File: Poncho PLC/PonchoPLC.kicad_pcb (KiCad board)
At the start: 2 copper layers, 85.7 x 137.2 mm, 137 parts, among them J1 I2C, J10 TB_1X3, J11 TB_1X3, J2 RS-232, J3 TB_1X3, J4 TB_1X3, J5 TB_1X2, J6 TB_1X2, J7 TB_1X2, J8 TB_1X3, J9 TB_1X3, K1 RELAY_C, K2 RELAY_C, K3 RELAY_C, K4 RELAY_C, P1 CONN_02X20, P10 CONN_01X20, P11 CONN_01X20, P12 CONN_01X06, P13 CONN_01X06, P14 CONN_02X12, P15 CONN_02X12, P16 CONN_02X12, P17 CONN_02X12, P18 CONN_01X12, P19 CONN_01X12, P2 CONN_01X20, P20 CONN_01X12, P21 CONN_01X12, P3 CONN_02X20, P4 CONN_02X20, P5 CONN_01X19, P6 CONN_02X20, P7 CONN_01X20, P8 CONN_02X20, P9 CONN_02X20, Q1 FQT13N06L, Q2 FQT13N06L, Q3 FQT13N06L, Q4 FQT13N06L, Q5 2N7002, Q6 2N7002, Q7 2N7002, Q8 2N7002, U1 TLP627-4, U2 TLP627-4, U3 MCP1416, U4 MCP1416, U5 MCP1416, U6 MCP1416

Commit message: Borro pistas y footprints del modelo, edito textos y separo componentes automáticamente por hojas.
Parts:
- removed G***: LOGO, Poncho_Esqueleto:Logo_Poncho
- removed G***: Logo_EDU-CIAA, Poncho_Esqueleto:Logo_EDU-CIAA
- removed G101: Logo_OSHWA, Poncho_Esqueleto:Logo_OSHWA
- removed P1, P3, P4, P6, P8, P9: CONN_02X20, Pin_Headers:Pin_Header_Straight_2x20
- removed P10, P11: CONN_01X20, Pin_Headers:Pin_Header_Straight_1x20
- removed P12, P13: CONN_01X06, mod:bornier6
- removed P14, P15, P16, P17: CONN_02X12, Pin_Headers:Pin_Header_Straight_2x12
- removed P18, P19, P20, P21: CONN_01X12, Pin_Headers:Pin_Header_Straight_1x12
- removed P2, P7: CONN_01X20, Pin_Headers:Pin_Header_Straight_2x12
- removed P5: CONN_01X19, Pin_Headers:Pin_Header_Straight_1x19
- moved R11 273.2 mm to (363.0, 54.8)
- moved R25 271.4 mm to (358.8, 50.3)
- moved R20 271.3 mm to (363.0, 59.3)
- moved R18 267.7 mm to (357.6, 56.2)
- moved D1 266.0 mm to (353.1, 50.9)
- moved R15 265.8 mm to (357.6, 60.7)
- moved R4 264.0 mm to (357.6, 65.2)
- moved R12 262.9 mm to (352.2, 56.2)
- moved R26 260.9 mm to (352.2, 60.7)
- moved D3 260.7 mm to (347.1, 50.9)
- moved R14 259.0 mm to (352.2, 65.2)
- moved R19 258.0 mm to (346.8, 56.2)
- moved R9 257.2 mm to (352.2, 69.7)
- moved R23 256.0 mm to (346.8, 60.7)
- moved R5 254.1 mm to (346.8, 65.2)
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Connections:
- net /Entradas Optoacopladas/COM renamed GNDD
- net /Salidas Digitales/MOS4 renamed Net-(JP2-Pad2)
- net /Salidas Digitales/MOS5 renamed Net-(JP1-Pad2)
- net /Salidas Digitales/MOS6 renamed Net-(JP3-Pad2)
- net /Salidas Digitales/MOS7 renamed Net-(JP4-Pad2)
- DS1 pad 10: Net-(DS1-Pad10) -> (no net)
- DS1 pad 7: Net-(DS1-Pad7) -> (no net)
- DS1 pad 8: Net-(DS1-Pad8) -> (no net)
- DS1 pad 9: Net-(DS1-Pad9) -> (no net)
- U2 pad 10: Net-(U2-Pad10) -> (no net)
- U2 pad 7: Net-(U2-Pad7) -> (no net)
- U2 pad 8: Net-(U2-Pad8) -> (no net)
- U2 pad 9: Net-(U2-Pad9) -> (no net)
- U3 pad 1: Net-(U3-Pad1) -> (no net)
- U4 pad 1: Net-(U4-Pad1) -> (no net)
- U5 pad 1: Net-(U5-Pad1) -> (no net)
- U6 pad 1: Net-(U6-Pad1) -> (no net)
- XA1 pad 11: /Conector del Poncho/ADC2 -> (no net)
- XA1 pad 13: /Conector del Poncho/ADC1 -> (no net)
- XA1 pad 15: /Conector del Poncho/DAC -> (no net)
- XA1 pad 17: +3.3VADC -> (no net)
- XA1 pad 27: /Conector del Poncho/RD -> (no net)
- XA1 pad 29: /Conector del Poncho/TD -> (no net)
- XA1 pad 3: /Conector del Poncho/RESET -> (no net)
- XA1 pad 41: +3.3VP -> (no net)
- XA1 pad 42: +5VP -> (no net)
- XA1 pad 44: /Conector del Poncho/RXD1 -> (no net)
- XA1 pad 46: /Conector del Poncho/TXEN -> (no net)
- XA1 pad 48: /Conector del Poncho/MDC -> (no net)
- XA1 pad 49: /Conector del Poncho/RXD0 -> (no net)
- XA1 pad 5: /Conector del Poncho/ISP -> (no net)
- XA1 pad 50: /Conector del Poncho/CRS -> (no net)
- XA1 pad 52: /Conector del Poncho/MDIO -> (no net)
- XA1 pad 54: /Conector del Poncho/TXD0 -> (no net)
- XA1 pad 55: /Conector del Poncho/RCLK -> (no net)
- XA1 pad 56: /Conector del Poncho/TXD1 -> (no net)
- XA1 pad 58: /Conector del Poncho/MISO -> (no net)
- XA1 pad 6: /Conector del Poncho/WAKEUP -> (no net)
- XA1 pad 60: /Conector del Poncho/spiSCK -> (no net)
- XA1 pad 61: /Conector del Poncho/MOSI -> (no net)
- XA1 pad 80: /Conector del Poncho/GPIO8 -> (no net)
- XA1 pad 9: /Conector del Poncho/ADC3 -> (no net)
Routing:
- net GND: track 336.4 -> 0.00 mm
- net +5VP: track 64.0 -> 0.00 mm
- net +5V: track 55.4 -> 0.00 mm
- net +3.3VP: track 54.0 -> 0.00 mm
- net +3.3V: track 52.0 -> 0.00 mm
- net GNDA: track 29.5 -> 0.00 mm
- net +3.3VADC: track 14.3 -> 0.00 mm
- net /Circuito Principal/F3: track 11.5 -> 0.00 mm
- net /Circuito Principal/TXD: track 11.5 -> 0.00 mm
- net /Circuito Principal/TD: track 11.5 -> 0.00 mm
- net /Circuito Principal/SDA: track 11.5 -> 0.00 mm
- net /Circuito Principal/SCL: track 11.5 -> 0.00 mm
- net /Circuito Principal/RXD: track 11.5 -> 0.00 mm
- net /Circuito Principal/RESET: track 11.5 -> 0.00 mm
- net /Circuito Principal/RD: track 11.5 -> 0.00 mm
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- removed copper zone on B.Cu, net GND
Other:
- board text added: "PONCHO PLC http://www.proyecto-ciaa.com.ar/"
- board text added: "STACK-UP PCB de xx capas COMPLETAR Stackup"
- board text removed: "PONCHO GRANDE http://www.proyecto-ciaa.com.ar/"

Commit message: Netlist y librería de footprint del proyecto
Generación y carga del archivo de conexiones del proyecto.
Se creo la librería de footprint propia del proyecto y se eliminó las
librerias que se utilizaron de soporte en la etapa inicial.
Se reemplazaron las líneas "model " por "model
${KIPRJMOD}/footprints/EESTN5.3dshapes/" pertenecientes al archivo
.kicad_pcb del proyecto para que se puedan visualizar correctamente los
modelos 3D.
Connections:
- DS1 pad 10: (no net) -> Net-(DS1-Pad10)
- DS1 pad 7: (no net) -> Net-(DS1-Pad7)
- DS1 pad 8: (no net) -> Net-(DS1-Pad8)
- DS1 pad 9: (no net) -> Net-(DS1-Pad9)
- U2 pad 10: (no net) -> Net-(U2-Pad10)
- U2 pad 7: (no net) -> Net-(U2-Pad7)
- U2 pad 8: (no net) -> Net-(U2-Pad8)
- U2 pad 9: (no net) -> Net-(U2-Pad9)
- U3 pad 1: (no net) -> Net-(U3-Pad1)
- U4 pad 1: (no net) -> Net-(U4-Pad1)
- U5 pad 1: (no net) -> Net-(U5-Pad1)
- U6 pad 1: (no net) -> Net-(U6-Pad1)
- XA1 pad 11: (no net) -> /Conector del Poncho/ADC2
- XA1 pad 13: (no net) -> /Conector del Poncho/ADC1
- XA1 pad 15: (no net) -> /Conector del Poncho/DAC
- XA1 pad 17: (no net) -> +3.3VADC
- XA1 pad 27: (no net) -> /Conector del Poncho/RD
- XA1 pad 29: (no net) -> /Conector del Poncho/TD
- XA1 pad 3: (no net) -> /Conector del Poncho/RESET
- XA1 pad 41: (no net) -> +3.3VP
- XA1 pad 42: (no net) -> +5VP
- XA1 pad 44: (no net) -> /Conector del Poncho/RXD1
- XA1 pad 46: (no net) -> /Conector del Poncho/TXEN
- XA1 pad 48: (no net) -> /Conector del Poncho/MDC
- XA1 pad 49: (no net) -> /Conector del Poncho/RXD0
- XA1 pad 5: (no net) -> /Conector del Poncho/ISP
- XA1 pad 50: (no net) -> /Conector del Poncho/CRS
- XA1 pad 52: (no net) -> /Conector del Poncho/MDIO
- XA1 pad 54: (no net) -> /Conector del Poncho/TXD0
- XA1 pad 55: (no net) -> /Conector del Poncho/RCLK
- XA1 pad 56: (no net) -> /Conector del Poncho/TXD1
- XA1 pad 58: (no net) -> /Conector del Poncho/MISO
- XA1 pad 6: (no net) -> /Conector del Poncho/WAKEUP
- XA1 pad 60: (no net) -> /Conector del Poncho/spiSCK
- XA1 pad 61: (no net) -> /Conector del Poncho/MOSI
- XA1 pad 80: (no net) -> /Conector del Poncho/GPIO8
- XA1 pad 9: (no net) -> /Conector del Poncho/ADC3
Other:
- board text removed: "STACK-UP PCB de xx capas COMPLETAR Stackup"

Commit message: Avance posicionamiento
Posicionamiento de las salidas digitales a relé.
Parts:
- moved Q6 249.2 mm to (44.3, 51.0), turned to 90 degrees
- moved R39 247.1 mm to (48.2, 51.0), turned to 270 degrees
- moved D18 242.2 mm to (43.9, 109.7), turned to 270 degrees
- moved Q8 239.3 mm to (44.3, 67.6), turned to 90 degrees
- moved R41 235.9 mm to (45.3, 55.5), turned to 180 degrees
- moved D17 229.7 mm to (46.8, 76.7), turned to 90 degrees
- moved J10 228.9 mm to (16.4, 103.2), turned to 270 degrees
- moved R45 228.0 mm to (45.3, 72.1), turned to 180 degrees
- moved R40 227.8 mm to (45.3, 88.5), turned to 180 degrees
- moved D15 225.0 mm to (43.9, 60.1), turned to 270 degrees
- moved Q7 222.4 mm to (44.3, 100.4), turned to 90 degrees
- moved J9 221.4 mm to (16.4, 72.7), turned to 270 degrees
- moved J8 219.0 mm to (16.4, 57.4), turned to 270 degrees
- moved R43 218.9 mm to (48.2, 67.6), turned to 270 degrees
- moved D13 218.0 mm to (46.8, 60.1), turned to 90 degrees
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- renumbered D19 to D111, K3 to K11

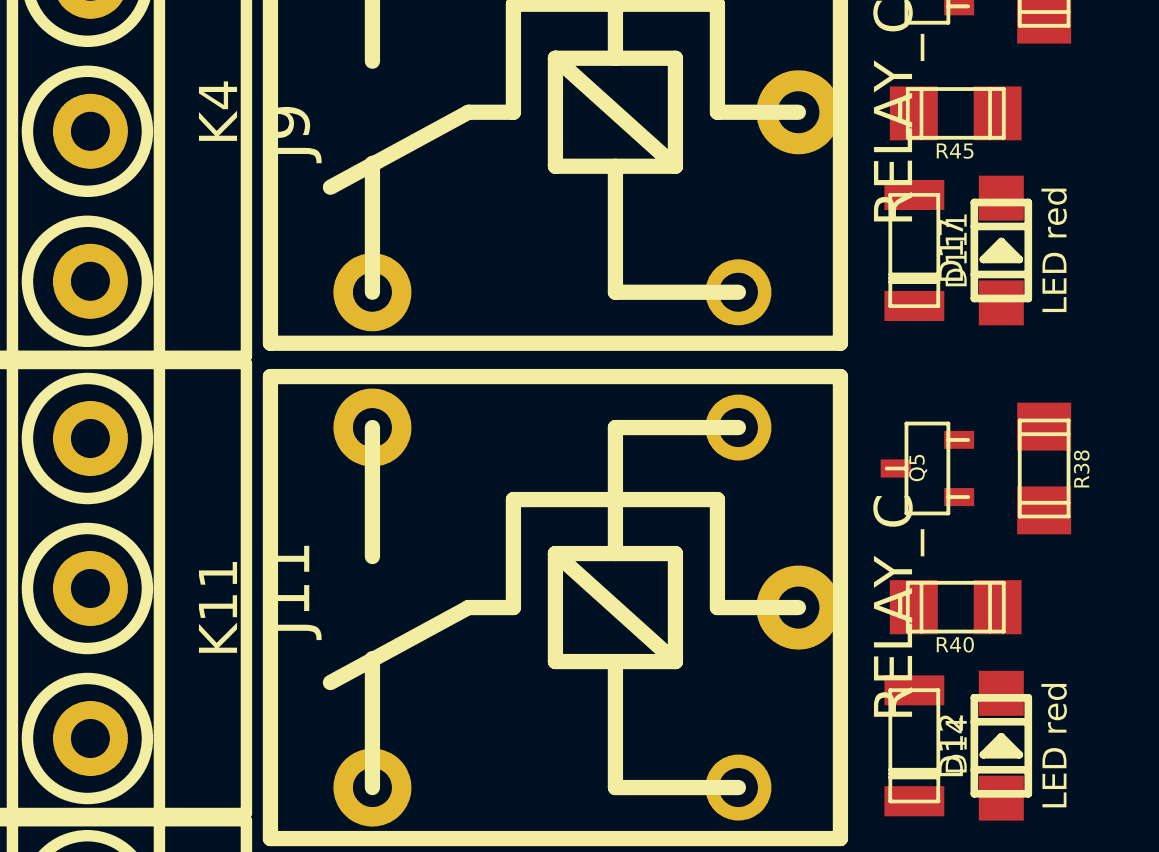
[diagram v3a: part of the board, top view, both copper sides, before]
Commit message: Cambio SCH
Se modificaron algunas etiquetas para beneficiar el routeo del pcb en la
conexión Rele-Bornera.
Se actualizaron las referencias de las huellas de la librería anterior a
la actual, para lograr compatibilidad en el netlist y poder cargarlo al
pcb.
Se actualizaron los filtros de búsqueda de huellas en algunos
componentes de la librería de sch.
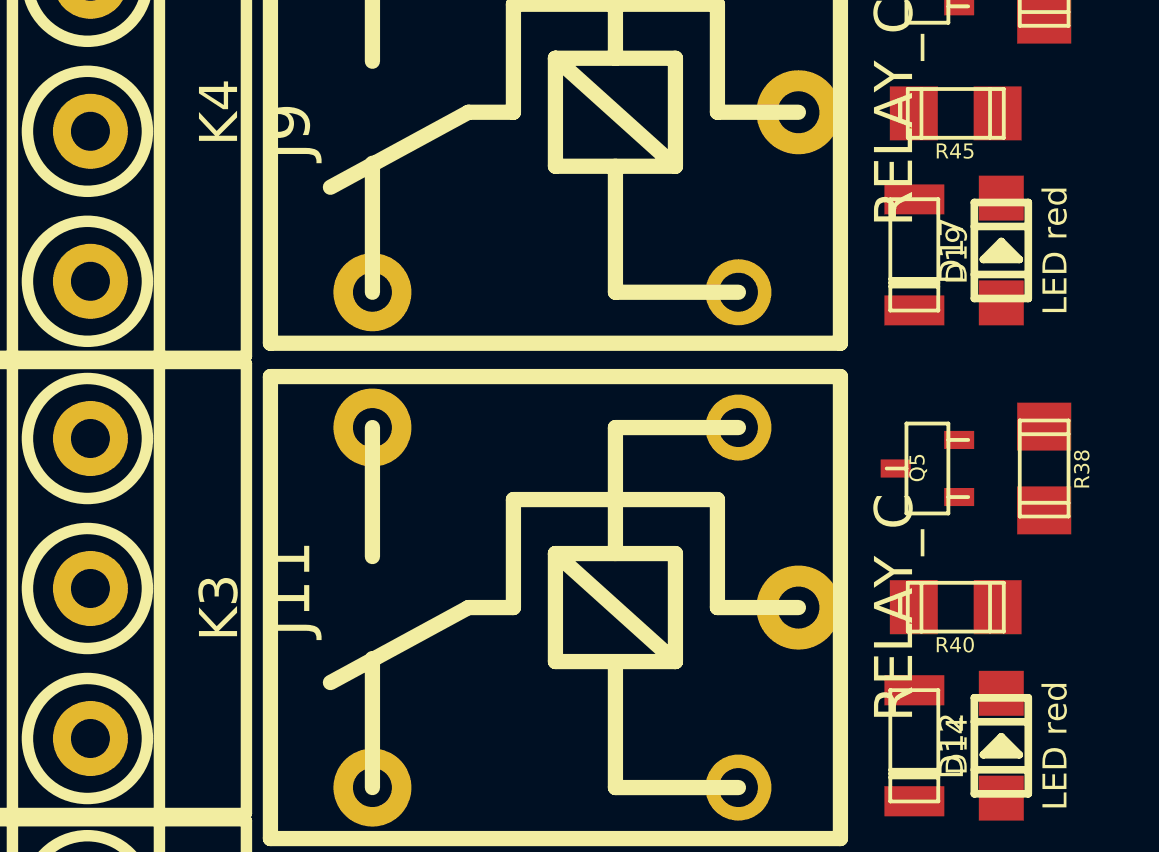
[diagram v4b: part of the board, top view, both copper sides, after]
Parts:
- removed D111: LL4148, EESTN5:SOD80C
- removed K11: RELAY_C, EESTN5:Relay_C
- added D19: LL4148, Poncho-PLC:SOD80C, F.Cu at (43.9, 76.8)
- added K3: RELAY_C, Poncho-PLC:Relay_C, F.Cu at (31.9, 88.6)
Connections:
- J10 pad 1: /Salidas Digitales/NC1C -> /Salidas Digitales/NO1C
- J10 pad 2: /Salidas Digitales/NO1C -> /Salidas Digitales/C1C
- J10 pad 3: /Salidas Digitales/C1C -> /Salidas Digitales/NC1C
- J11 pad 1: /Salidas Digitales/NC1D -> /Salidas Digitales/NO1D
- J11 pad 2: /Salidas Digitales/NO1D -> /Salidas Digitales/C1D
- J11 pad 3: /Salidas Digitales/C1D -> /Salidas Digitales/NC1D
- J8 pad 1: /Salidas Digitales/NC1A -> /Salidas Digitales/NO1A
- J8 pad 2: /Salidas Digitales/NO1A -> /Salidas Digitales/C1A
- J8 pad 3: /Salidas Digitales/C1A -> /Salidas Digitales/NC1A
- J9 pad 1: /Salidas Digitales/NC1B -> /Salidas Digitales/NO1B
- J9 pad 2: /Salidas Digitales/NO1B -> /Salidas Digitales/C1B
- J9 pad 3: /Salidas Digitales/C1B -> /Salidas Digitales/NC1B

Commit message: Avance posicionamiento
Posicione las borneras de las entradas digitales.
Arregle el footprint de las borneras para que tengan un pitch de 100mils
Cambie a bottom layer algunos componentes para acercarme a un tamaño de
placa de 150X100mm
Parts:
- D17, D18, Q7, Q8, R10, R11, R12, R13, R14, R15, R2, R3, R4, R44, R45, R5, R6, R7, R8, R9: moved to B.Cu
- J3, J4: footprint EESTN5:BORNERA3 -> Poncho-PLC:BORNERA3
- J5: footprint EESTN5:BORNERA2 -> Poncho-PLC:BORNERA2
- J6, J7: footprint EESTN5:BORNERA3 -> Poncho-PLC:BORNERA2
- moved J6 214.3 mm to (47.2, 147.6), turned to 270 degrees
- moved J7 196.8 mm to (47.1, 137.4), turned to 270 degrees
- moved R11 195.0 mm to (180.9, 124.4)
- moved R4 187.2 mm to (180.9, 126.9)
- moved R9 183.2 mm to (180.9, 134.4)
- moved R12 182.6 mm to (180.9, 119.3)
- moved R15 182.0 mm to (180.9, 104.1)
- moved R14 177.0 mm to (180.8, 109.2)
- moved R5 175.3 mm to (180.9, 121.8)
- moved R10 174.9 mm to (180.9, 129.4)
- moved R2 170.2 mm to (180.9, 136.9)
- moved R7 166.8 mm to (180.9, 111.9)
- moved R3 163.0 mm to (180.9, 131.9)
- moved J5 157.9 mm to (187.7, 103.8), turned to 90 degrees
- moved R8 156.3 mm to (180.9, 106.6)
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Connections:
- D1 pad 2: /Conector del Poncho/COL0 -> /Conector del Poncho/COL1
- D2 pad 2: /Conector del Poncho/COL1 -> /Conector del Poncho/COL2
- D3 pad 2: /Conector del Poncho/COL2 -> /Entradas Optoacopladas/DIN2
- D5 pad 2: /Entradas Optoacopladas/DIN4 -> /Conector del Poncho/COL0
- R17 pad 1: /Conector del Poncho/COL0 -> /Conector del Poncho/COL1
- R19 pad 1: /Conector del Poncho/COL1 -> /Conector del Poncho/COL2
- R21 pad 1: /Conector del Poncho/COL2 -> /Entradas Optoacopladas/DIN2
- R25 pad 1: /Entradas Optoacopladas/DIN4 -> /Conector del Poncho/COL0
- U1 pad 12: /Conector del Poncho/COL2 -> /Entradas Optoacopladas/DIN2
- U1 pad 14: /Conector del Poncho/COL1 -> /Conector del Poncho/COL2
- U1 pad 16: /Conector del Poncho/COL0 -> /Conector del Poncho/COL1
- U2 pad 16: /Entradas Optoacopladas/DIN4 -> /Conector del Poncho/COL0
- XA1 pad 33: /Entradas Optoacopladas/DIN3 -> /Entradas Optoacopladas/DIN2
- XA1 pad 36: /Entradas Optoacopladas/DIN4 -> /Entradas Optoacopladas/DIN3
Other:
- board size 85.7 x 137.2 mm -> 150 x 137.2 mm

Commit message: Avance posicionamiento & Dimensión del poncho
Se avanzo en el posicionamiento de las entradas.
Se esta evaluando la dimensión del poncho y la posición de los agujeros
de sujeción.
A partir de ahora el diseño esta a cargo del Alumno Ignacio Vetrano
(E.E.S.T. N°5 - 5to 5ta)
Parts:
- D14, D15, Q5, Q6, R40, R41, U3: moved to B.Cu
- J10, J11, J8, J9: footprint EESTN5:BORNERA3 -> Poncho-PLC:BORNERA3
- moved D9 220.3 mm to (57.6, 145.0)
- moved R30 218.6 mm to (64.0, 146.1)
- moved Q1 213.1 mm to (61.1, 141.7)
- moved R34 209.2 mm to (57.1, 149.7), turned to 90 degrees
- moved TH1 189.2 mm to (65.6, 150.2)
- moved JP2 131.2 mm to (60.2, 154.7)
- moved U3 129.6 mm to (60.2, 149.4)
- moved R38 17.6 mm to (75.1, 106.9)
- moved D16 16.6 mm to (75.1, 99.0)
- moved D18 16.6 mm to (75.2, 99.1)
- moved Q7 16.6 mm to (75.3, 89.2)
- moved R42 16.6 mm to (75.2, 90.6)
- moved R44 16.6 mm to (75.2, 93.8)
- moved D14 16.5 mm to (75.1, 115.7)
- moved D12 16.5 mm to (75.1, 115.4)
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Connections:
- TH1 pad 2: Net-(J6-Pad1) -> Net-(J6-Pad2)
- TH2 pad 2: Net-(J6-Pad2) -> Net-(J6-Pad1)
- TH3 pad 2: Net-(J7-Pad1) -> Net-(J7-Pad2)
- TH4 pad 2: Net-(J7-Pad2) -> Net-(J7-Pad1)
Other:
- net class Default: via_dia 0.6 -> 1.5; via_drill 0.4 -> 0.5
- rule via_min_drill: 0.3 -> 0.5
- rule via_min_size: 0.4 -> 1.5

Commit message: tamaño placa
Se ajusto el tamaño de la placa a 100x150mm.
Avance en posicionamiento.
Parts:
- U4: moved to B.Cu
- moved U4 226.9 mm to (65.3, 106.9), turned to 270 degrees
- moved C6 220.7 mm to (65.3, 112.7), turned to 180 degrees
- moved R35 216.6 mm to (61.3, 118.9), turned to 270 degrees
- moved C1 214.1 mm to (58.4, 119.1), turned to 270 degrees
- moved R31 213.0 mm to (69.4, 117.7), turned to 90 degrees
- moved D10 198.9 mm to (65.2, 120.3)
- moved Q2 198.6 mm to (58.3, 113.2), turned to 90 degrees
- moved R32 197.5 mm to (77.5, 133.5), turned to 90 degrees
- moved C5 186.6 mm to (72.0, 128.5), turned to 90 degrees
- moved JP1 184.3 mm to (65.2, 115.5), turned to 180 degrees
- moved TH2 176.6 mm to (55.2, 118.9), turned to 90 degrees
- moved C2 158.0 mm to (65.3, 109.9)
- moved Q4 97.4 mm to (300.8, 95.4)
- moved C3 97.4 mm to (298.5, 114.9)
- moved C8 97.4 mm to (302.2, 105.3)
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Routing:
- net +5V: track 0.00 -> 57.4 mm
- net GND: track 0.00 -> 36.3 mm, vias 0 -> 1
- net /Salidas Digitales/C1C: track 0.00 -> 24.5 mm
- net /Salidas Digitales/C1D: track 0.00 -> 24.2 mm
- net /Salidas Digitales/C1B: track 0.00 -> 24.0 mm
- net /Salidas Digitales/C1A: track 0.00 -> 23.6 mm
- net Net-(JP1-Pad2): track 0.00 -> 15.7 mm
- net Net-(J6-Pad1): track 0.00 -> 13.9 mm
- net /Salidas Digitales/DOUT5: track 0.00 -> 13.7 mm
- net Net-(Q2-Pad2): track 0.00 -> 11.1 mm
- net /Salidas Digitales/NC1C: track 0.00 -> 10.7 mm
- net Net-(Q1-Pad2): track 0.00 -> 10.5 mm
- net /Salidas Digitales/NC1D: track 0.00 -> 10.4 mm
- net /Salidas Digitales/NC1B: track 0.00 -> 10.2 mm
- net /Salidas Digitales/NO1C: track 0.00 -> 9.95 mm
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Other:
- board size 150 x 137.2 mm -> 150 x 99.7 mm
- net class Default: clearance 0.508 -> 0.254; via_dia 1.5 -> 1.016
- rule trace_clearance: 0.508 -> 0.254
- rule trace_min: 0.2 -> 0.2032
- rule via_min_size: 1.5 -> 1.016

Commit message: Avance posicionamiento
Se avanzo en el posicionamiento de componentes.
Se actualizo el modelo 3D de varios componentes.
Se agregaron los logos de la escuela y de Open Hardware.
Falta actualizar las librerias del repositorio y las rutas relativas de
los modelos 3D para que la vista 3D sea portable a cualquier pc.
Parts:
- added G1: LOGO, EESTN5:LOGO_EESTN5, F.Cu at (179.0, 66.6)
- added G2: LOGO, Logo_silk_OSHW_12x13mm, F.Cu at (178.4, 52.8)
- C1, C2, C3, C4, C5, C6, C7, C8: footprint EESTN5:C_1206 -> Poncho-PLC:C_1206
- D1, D10, D11, D12, D13, D16, D2, D3, D4, D5, D6, D7, D8, D9: footprint EESTN5:LED_1206 -> Poncho-PLC:LED_1206
- D14, D15, D18: footprint EESTN5:SOD80C -> Poncho-PLC:SOD80C
- D17: footprint EESTN5:LED_1206 -> Poncho-PLC:LED_1206; moved to F.Cu
- D19: moved to B.Cu
- DS1: footprint EESTN5:LCD_16x2 -> Poncho-PLC:LCD_16x2
- J1: footprint EESTN5:HEADER-4H -> EESTN5:JST-4V
- J2: footprint EESTN5:HEADER-4H -> Poncho-PLC:HEADER-4H; moved to B.Cu
- JP1, JP2, JP3, JP4: footprint EESTN5:Pin_strip_2 -> Poncho-PLC:Pin_strip_2
- K1, K2, K4: footprint EESTN5:Relay_C -> Poncho-PLC:Relay_C
- Q1, Q2, Q3, Q4: footprint EESTN5:SOT-223 -> Poncho-PLC:SOT-223; moved to B.Cu
- Q5, Q6, Q7, Q8: footprint EESTN5:SOT23 -> Poncho-PLC:SOT23
- R1, R17, R19, R21, R23, R25, R27, R29, R30, R31, R32, R33: footprint EESTN5:R_1206 -> Poncho-PLC:R_1206; moved to B.Cu
- R10, R11, R12, R13, R14, R15, R16, R18, R2, R20, R22, R24, R26, R28, R3, R34, R35, R36, R37, R38, R39, R4, R40, R41, R42, R43, R44, R45, R5, R6, R7, R8, R9: footprint EESTN5:R_1206 -> Poncho-PLC:R_1206
- RV1: footprint EESTN5:TRIMER_V -> Poncho-PLC:TRIMER_V
- TH1, TH2, TH3, TH4: footprint EESTN5:PTC_1210 -> Poncho-PLC:PTC_1210
- U1, U2: footprint EESTN5:DIP_16-300_socket -> Poncho-PLC:DIP_16-300_socket
- U3, U4: footprint EESTN5:SOT-23-5 -> Poncho-PLC:SOT-23-5
- U5, U6: footprint EESTN5:SOT-23-5 -> Poncho-PLC:SOT-23-5; moved to B.Cu
- XA1: footprint mod:poncho_grande -> Poncho-PLC:poncho_grande
- moved Q4 246.4 mm to (58.0, 137.7), turned to 270 degrees
- moved C8 243.9 mm to (60.5, 137.7), turned to 270 degrees
- moved C3 241.1 mm to (57.9, 130.0), turned to 270 degrees
- moved JP4 234.9 mm to (70.4, 137.7), turned to 270 degrees
- moved U6 229.3 mm to (65.2, 137.7)
- moved R37 227.8 mm to (65.2, 136.4)
- moved C7 216.0 mm to (60.5, 130.0), turned to 270 degrees
- moved D11 215.8 mm to (65.2, 131.3), turned to 180 degrees
- moved D8 206.1 mm to (65.2, 138.9), turned to 180 degrees
- moved R33 201.7 mm to (85.5, 135.9), turned to 90 degrees
- moved U5 201.1 mm to (65.2, 130.0)
- moved D1 199.1 mm to (175.3, 128.3), turned to 180 degrees
- moved R18 197.8 mm to (175.3, 125.7)
- moved R25 197.5 mm to (166.7, 105.4), turned to 90 degrees
- moved R19 195.2 mm to (166.7, 124.5), turned to 90 degrees
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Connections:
- net /Conector del Poncho/COL0 renamed /DIN4
- JP1 pad 1: /Salidas Digitales/DOUT5 -> /Salidas Digitales/DOUT4
- JP2 pad 1: /Salidas Digitales/DOUT4 -> /Salidas Digitales/DOUT5
- Q1 pad 1: Net-(JP2-Pad2) -> Net-(JP1-Pad2)
- Q2 pad 1: Net-(JP1-Pad2) -> Net-(JP2-Pad2)
- R34 pad 2: Net-(JP2-Pad2) -> Net-(JP1-Pad2)
- R35 pad 2: Net-(JP1-Pad2) -> Net-(JP2-Pad2)
- TH1 pad 2: Net-(J6-Pad2) -> Net-(J6-Pad1)
- TH2 pad 2: Net-(J6-Pad1) -> Net-(J6-Pad2)
- TH3 pad 2: Net-(J7-Pad2) -> Net-(J7-Pad1)
- TH4 pad 2: Net-(J7-Pad1) -> Net-(J7-Pad2)
- U3 pad 5: Net-(JP2-Pad2) -> Net-(JP1-Pad2)
- U4 pad 5: Net-(JP1-Pad2) -> Net-(JP2-Pad2)
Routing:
- net GND: track 36.3 -> 0.00 mm, vias 1 -> 0
- net Net-(JP1-Pad2): track 15.7 -> 0.00 mm
- net Net-(J6-Pad1): track 13.9 -> 0.00 mm
- net /Salidas Digitales/DOUT5: track 13.7 -> 0.00 mm
- net +5V: track 57.4 -> 45.3 mm
- net Net-(Q2-Pad2): track 11.1 -> 0.00 mm
- net Net-(Q1-Pad2): track 10.5 -> 0.00 mm
- net Net-(R14-Pad2): track 0.00 -> 8.31 mm
- net Net-(R13-Pad2): track 0.00 -> 8.18 mm
- net Net-(R15-Pad2): track 0.00 -> 8.13 mm
- net Net-(R2-Pad2): track 0.00 -> 8.11 mm
- net Net-(R10-Pad2): track 0.00 -> 8.11 mm
- net Net-(R11-Pad2): track 0.00 -> 8.10 mm
- net Net-(R12-Pad2): track 0.00 -> 8.02 mm
- net /Entradas Optoacopladas/IN5: track 0.00 -> 5.63 mm
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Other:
- board size 150 x 99.7 mm -> 150 x 100 mm
- board text removed: "3.3V"
- board text removed: "5V"
- board text removed: "GND"
